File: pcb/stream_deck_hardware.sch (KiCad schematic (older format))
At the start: 33 parts, among them J1 Conn_BOOT, J2 USB_C_Receptacle_USB2.0, J3 Conn_01x04_Male, J4 Conn_01x04_Male, U1 LF33_TO252, U2 STM32F401RCTx, U3 74LVC1G332, U4 AT24CS02-STUM, U5 AT24CS02-STUM, Y1 Crystal_Small

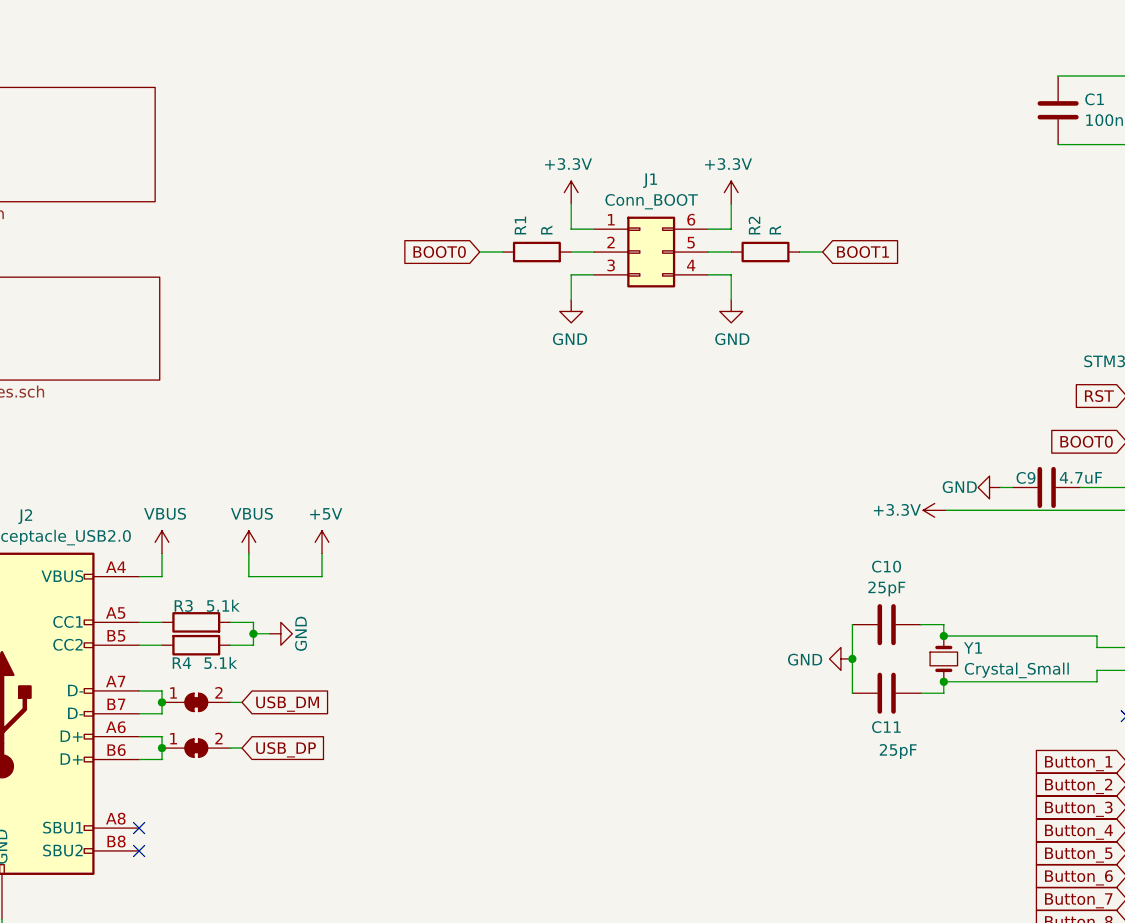
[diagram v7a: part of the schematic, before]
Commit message: Components placement
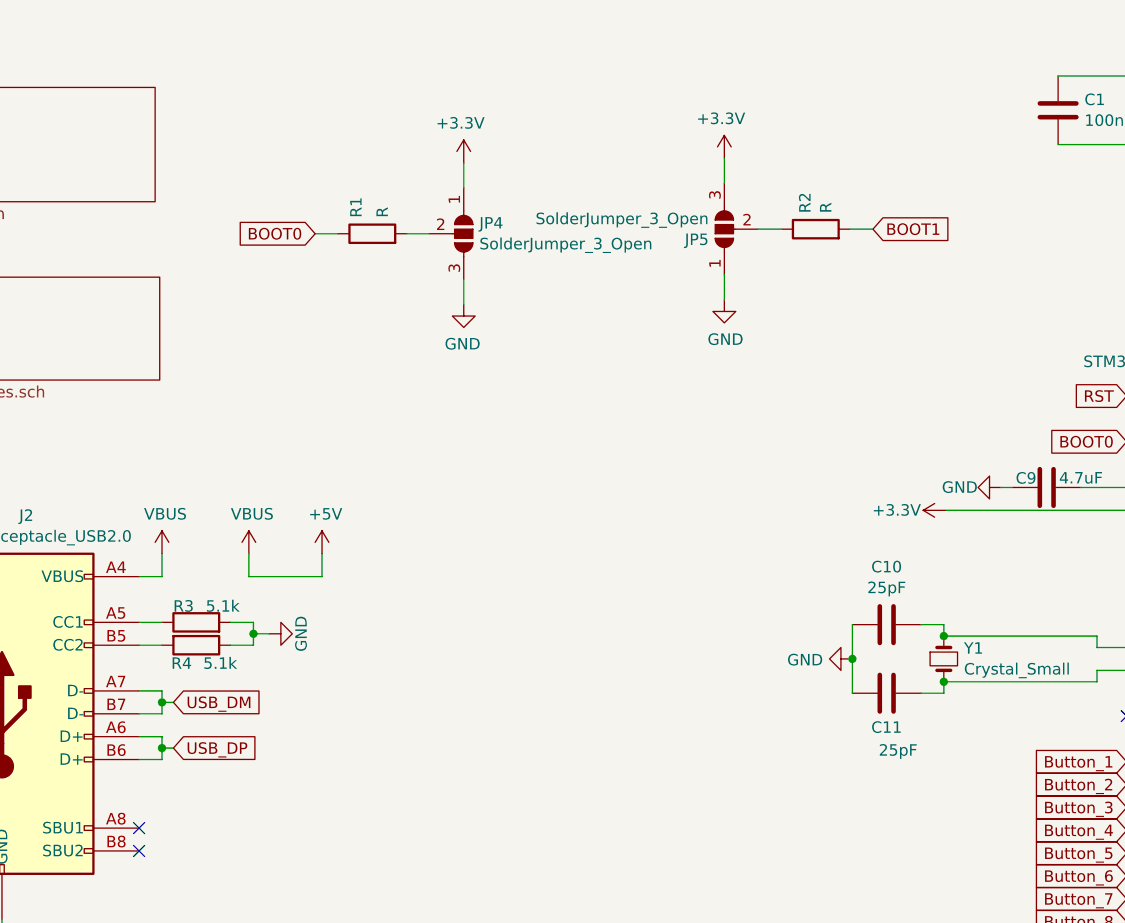
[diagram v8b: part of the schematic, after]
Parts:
- removed J1: Conn_BOOT, Connector_PinHeader_2.54mm:PinHeader_2x03_P2.54mm_Vertical, symbol Connector_Generic:Conn_02x03_Counter_Clockwise
- removed JP1, JP2: SolderJumper_2_Bridged, Jumper:SolderJumper-2_P1.3mm_Bridged2Bar_RoundedPad1.0x1.5mm, symbol Jumper:SolderJumper_2_Bridged
- added JP4, JP5: SolderJumper_3_Open, Jumper:SolderJumper-3_P1.3mm_Bridged2Bar12_RoundedPad1.0x1.5mm_NumberLabels, symbol Jumper:SolderJumper_3_Open
- J3: footprint Connector_PinHeader_2.54mm:PinHeader_1x04_P2.54mm_Vertical -> Connector_Wire:SolderWire-0.1sqmm_1x04_P3.6mm_D0.4mm_OD1mm_Relief
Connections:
- net +3V3: now also JP4.1 (A), JP5.3 (B)
- net GND: now also JP4.3 (B), JP5.1 (A)
- net USB_DM: now also J2.A7 (D-), J2.B7 (D-)
- net USB_DP: now also J2.A6 (D+), J2.B6 (D+)
- net at R1.2: now also JP4.2 (C)
- net at R2.1: now also JP5.2 (C)
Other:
- moved on the sheet: R1, R2
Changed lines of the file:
@@
 Text GLabel 7550 4150 2    50   Input ~ 0
 BOOT1
-Text GLabel 3420 1620 0    50   Input ~ 0
+Text GLabel 2700 1540 0    50   Input ~ 0
 BOOT0
-$Comp
-L Connector_Generic:Conn_02x03_Counter_Clockwise J1
-U 1 1 6197877E
-P 4120 1620
-F 0 "J1" H 4170 1937 50  0000 C CNN
-F 1 "Conn_BOOT" H 4170 1846 50  0000 C CNN
-F 2 "Connector_PinHeader_2.54mm:PinHeader_2x03_P2.54mm_Vertical" H 4120 1620 50  0001 C CNN
-F 3 "~" H 4120 1620 50  0001 C CNN
-	1    4120 1620
-	1    0    0    -1
-$EndComp
 $Comp
 L power:GND #PWR09
 U 1 1 61986215
-P 4520 1830
-F 0 "#PWR09" H 4520 1580 50  0001 C CNN
-F 1 "GND" H 4525 1657 50  0000 C CNN
-F 2 "" H 4520 1830 50  0001 C CNN
-F 3 "" H 4520 1830 50  0001 C CNN
-	1    4520 1830
-	1    0    0    -1
-$EndComp
-Wire Wire Line
-	4420 1720 4520 1720
-Wire Wire Line
-	4520 1720 4520 1830
+P 4490 1830
+F 0 "#PWR09" H 4490 1580 50  0001 C CNN
+F 1 "GND" H 4495 1657 50  0000 C CNN
+F 2 "" H 4490 1830 50  0001 C CNN
+F 3 "" H 4490 1830 50  0001 C CNN
+	1    4490 1830
+	1    0    0    -1
+$EndComp
+Wire Wire Line
+	4490 1720 4490 1830
 $Comp
 L power:GND #PWR08
 U 1 1 6198ABFD
-P 3820 1830
-F 0 "#PWR08" H 3820 1580 50  0001 C CNN
-F 1 "GND" H 3825 1657 50  0000 C CNN
-F 2 "" H 3820 1830 50  0001 C CNN
-F 3 "" H 3820 1830 50  0001 C CNN
-	1    3820 1830
+P 3350 1850
+F 0 "#PWR08" H 3350 1600 50  0001 C CNN
+F 1 "GND" H 3355 1677 50  0000 C CNN
+F 2 "" H 3350 1850 50  0001 C CNN
+F 3 "" H 3350 1850 50  0001 C CNN
+	1    3350 1850
 	-1   0    0    -1
 $EndComp
 Wire Wire Line
-	3920 1720 3820 1720
-Wire Wire Line
-	3820 1720 3820 1830
-Wire Wire Line
-	4520 1520 4520 1410
-Wire Wire Line
-	4420 1520 4520 1520
+	3350 1740 3350 1850
+Wire Wire Line
+	4490 1320 4490 1210
 $Comp
 L power:+3.3V #PWR07
 U 1 1 61995457
-P 4520 1410
-F 0 "#PWR07" H 4520 1160 50  0001 C CNN
-F 1 "+3.3V" H 4535 1583 50  0000 C CNN
-F 2 "" H 4520 1410 50  0001 C CNN
-F 3 "" H 4520 1410 50  0001 C CNN
-	1    4520 1410
+P 4490 1210
+F 0 "#PWR07" H 4490 960 50  0001 C CNN
+F 1 "+3.3V" H 4505 1383 50  0000 C CNN
+F 2 "" H 4490 1210 50  0001 C CNN
+F 3 "" H 4490 1210 50  0001 C CNN
+	1    4490 1210
 	-1   0    0    -1
 $EndComp
 Wire Wire Line
-	3920 1520 3820 1520
-Wire Wire Line
-	3820 1520 3820 1410
+	3350 1340 3350 1230
 $Comp
 L power:+3.3V #PWR06
 U 1 1 6199E8B3
-P 3820 1410
-F 0 "#PWR06" H 3820 1160 50  0001 C CNN
-F 1 "+3.3V" H 3835 1583 50  0000 C CNN
-F 2 "" H 3820 1410 50  0001 C CNN
-F 3 "" H 3820 1410 50  0001 C CNN
-	1    3820 1410
+P 3350 1230
+F 0 "#PWR06" H 3350 980 50  0001 C CNN
+F 1 "+3.3V" H 3365 1403 50  0000 C CNN
+F 2 "" H 3350 1230 50  0001 C CNN
+F 3 "" H 3350 1230 50  0001 C CNN
+	1    3350 1230
 	-1   0    0    -1
 $EndComp
-Text GLabel 4920 1620 2    50   Input ~ 0
+Text GLabel 5140 1520 2    50   Input ~ 0
 BOOT1
 Wire Wire Line
-	3820 1620 3920 1620
-Wire Wire Line
-	4420 1620 4520 1620
+	3100 1540 3200 1540
+Wire Wire Line
+	4640 1520 4740 1520
 $Comp
 L Connector:USB_C_Receptacle_USB2.0 J2
@@
 Wire Wire Line
 	2030 3840 1930 3840
-Text GLabel 2380 3590 2    50   Input ~ 0
+Text GLabel 2080 3590 2    50   Input ~ 0
 USB_DM
-Text GLabel 2380 3790 2    50   Input ~ 0
+Text GLabel 2080 3790 2    50   Input ~ 0
 USB_DP
 Wire Wire Line
@@
 L Device:R R2
 U 1 1 619882F0
-P 4670 1620
-F 0 "R2" H 4740 1666 50  0000 L CNN
-F 1 "R" H 4740 1575 50  0000 L CNN
-F 2 "Resistor_SMD:R_0603_1608Metric" V 4600 1620 50  0001 C CNN
-F 3 "~" H 4670 1620 50  0001 C CNN
-	1    4670 1620
-	0    -1   -1   0
-$EndComp
-Wire Wire Line
-	4820 1620 4920 1620
-Wire Wire Line
-	3420 1620 3520 1620
+P 4890 1520
+F 0 "R2" H 4960 1566 50  0000 L CNN
+F 1 "R" H 4960 1475 50  0000 L CNN
+F 2 "Resistor_SMD:R_0603_1608Metric" V 4820 1520 50  0001 C CNN
+F 3 "~" H 4890 1520 50  0001 C CNN
+	1    4890 1520
+	0    -1   -1   0
+$EndComp
+Wire Wire Line
+	5040 1520 5140 1520
+Wire Wire Line
+	2700 1540 2800 1540
 $Comp
 L Device:R R4
@@
 L Device:R R1
 U 1 1 61985051
-P 3670 1620
-F 0 "R1" H 3740 1690 50  0000 L CNN
-F 1 "R" H 3740 1575 50  0000 L CNN
-F 2 "Resistor_SMD:R_0603_1608Metric" V 3600 1620 50  0001 C CNN
-F 3 "~" H 3670 1620 50  0001 C CNN
-	1    3670 1620
+P 2950 1540
+F 0 "R1" H 3020 1610 50  0000 L CNN
+F 1 "R" H 3020 1495 50  0000 L CNN
+F 2 "Resistor_SMD:R_0603_1608Metric" V 2880 1540 50  0001 C CNN
+F 3 "~" H 2950 1540 50  0001 C CNN
+	1    2950 1540
 	0    -1   -1   0
 $EndComp
@@
 F 0 "J3" H 4792 5902 50  0000 R CNN
 F 1 "Conn_01x04_Male" H 4792 5993 50  0000 R CNN
-F 2 "Connector_PinHeader_2.54mm:PinHeader_1x04_P2.54mm_Vertical" H 4820 6020 50  0001 C CNN
+F 2 "Connector_Wire:SolderWire-0.1sqmm_1x04_P3.6mm_D0.4mm_OD1mm_Relief" H 4820 6020 50  0001 C CNN
 F 3 "~" H 4820 6020 50  0001 C CNN
 	1    4820 6020
@@
 Wire Wire Line
 	5120 6220 5120 6320
-$Comp
-L Jumper:SolderJumper_2_Bridged JP1
-U 1 1 61B00D59
-P 2180 3590
-F 0 "JP1" H 2180 3795 50  0001 C CNN
-F 1 "SolderJumper_2_Bridged" H 2180 3704 50  0001 C CNN
-F 2 "Jumper:SolderJumper-2_P1.3mm_Bridged2Bar_RoundedPad1.0x1.5mm" H 2180 3590 50  0001 C CNN
-F 3 "~" H 2180 3590 50  0001 C CNN
-	1    2180 3590
-	1    0    0    -1
-$EndComp
-Wire Wire Line
-	2030 3540 2030 3590
-Connection ~ 2030 3590
-Wire Wire Line
-	2030 3590 2030 3640
-$Comp
-L Jumper:SolderJumper_2_Bridged JP2
-U 1 1 61B0EE49
-P 2180 3790
-F 0 "JP2" H 2180 3995 50  0001 C CNN
-F 1 "SolderJumper_2_Bridged" H 2180 3904 50  0001 C CNN
-F 2 "Jumper:SolderJumper-2_P1.3mm_Bridged2Bar_RoundedPad1.0x1.5mm" H 2180 3790 50  0001 C CNN
-F 3 "~" H 2180 3790 50  0001 C CNN
-	1    2180 3790
-	1    0    0    -1
-$EndComp
-Wire Wire Line
-	2030 3740 2030 3790
-Connection ~ 2030 3790
-Wire Wire Line
-	2030 3790 2030 3840
-Wire Wire Line
-	2330 3790 2380 3790
-Wire Wire Line
-	2380 3590 2330 3590
+Wire Wire Line
+	2030 3790 2080 3790
+Wire Wire Line
+	2080 3590 2030 3590
 Wire Wire Line
 	2430 3240 2330 3240
@@
 Wire Wire Line
 	6250 2650 6050 2650
+$Comp
+L Jumper:SolderJumper_3_Open JP4
+U 1 1 61E76CC5
+P 3350 1540
+F 0 "JP4" V 3304 1608 50  0000 L CNN
+F 1 "SolderJumper_3_Open" V 3395 1608 50  0000 L CNN
+F 2 "Jumper:SolderJumper-3_P1.3mm_Bridged2Bar12_RoundedPad1.0x1.5mm_NumberLabels" H 3350 1540 50  0001 C CNN
+F 3 "~" H 3350 1540 50  0001 C CNN
+	1    3350 1540
+	0    1    1    0
+$EndComp
+$Comp
+L Jumper:SolderJumper_3_Open JP5
+U 1 1 61EA431B
+P 4490 1520
+F 0 "JP5" V 4444 1588 50  0000 L CNN
+F 1 "SolderJumper_3_Open" V 4535 1588 50  0000 L CNN
+F 2 "Jumper:SolderJumper-3_P1.3mm_Bridged2Bar12_RoundedPad1.0x1.5mm_NumberLabels" H 4490 1520 50  0001 C CNN
+F 3 "~" H 4490 1520 50  0001 C CNN
+	1    4490 1520
+	0    -1   -1   0
+$EndComp
+Wire Wire Line
+	2030 3540 2030 3590
+Wire Wire Line
+	2030 3740 2030 3790
+Connection ~ 2030 3590
+Wire Wire Line
+	2030 3590 2030 3640
+Connection ~ 2030 3790
+Wire Wire Line
+	2030 3790 2030 3840
 $EndSCHEMATC
